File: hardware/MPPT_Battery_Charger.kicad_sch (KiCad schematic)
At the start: 74 parts, among them Q24 SI7414DN-T1-E3, Q25 SI7414DN-T1-E3, Q5 SI2302DDS-T1-GE3, Q5 SI7414DN-T1-E3, Q6 SI7414DN-T1-E3, U22 BQ24650RVAT, U26 LMV321RIYLT, U28 LMV321RIYLT, U4 INA199C1DCKR

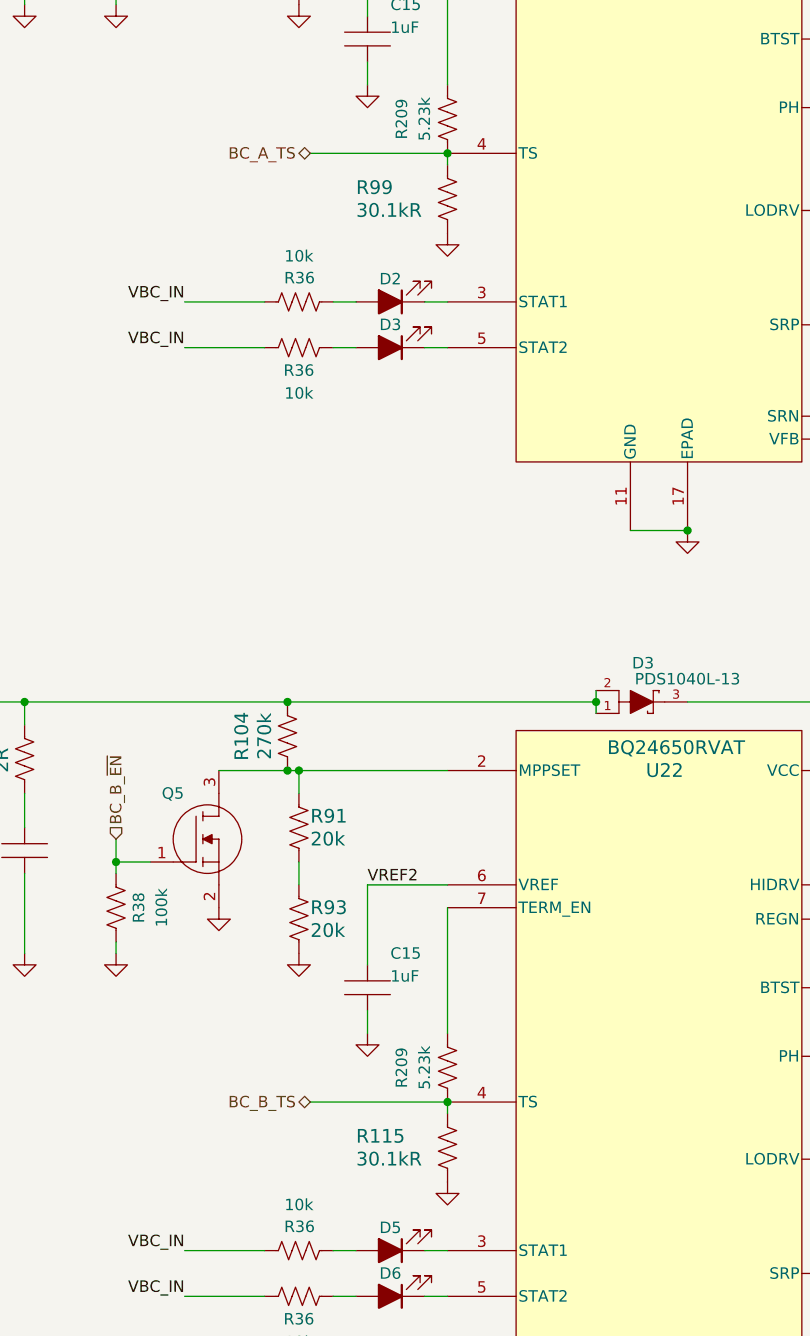
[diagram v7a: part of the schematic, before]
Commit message: hardware: Updating some footprints and 3D models.
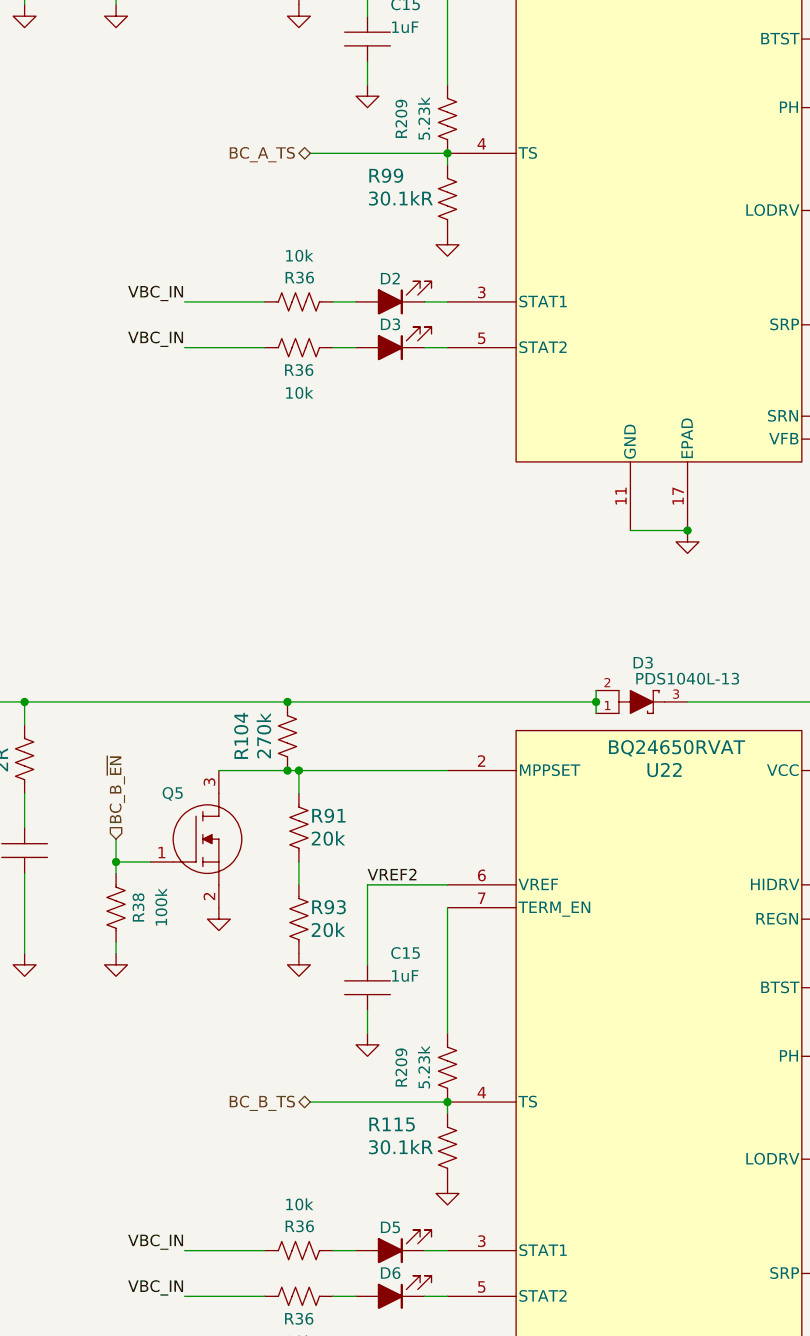
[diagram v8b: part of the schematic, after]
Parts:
- R115, R99: footprint RES_CRCW_0603_VIS -> footprints:CRCW060330K1FKEAHP
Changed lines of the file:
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@@
     )
   )
-  (symbol (lib_name "CRCW060330K1FKEAHP_1") (lib_id "CRCW060330K1FKEAHP:CRCW060330K1FKEAHP") (at 148.59 80.01 90) (unit 1)
+  (symbol (lib_id "CRCW060330K1FKEAHP:CRCW060330K1FKEAHP") (at 149.86 78.74 90) (unit 1)
     (in_bom yes) (on_board yes) (dnp no)
-    (property "Reference" "R99" (at 139.7 72.39 90)
+    (property "Reference" "R99" (at 140.97 71.12 90)
       (effects (font (size 1.524 1.524)) (justify right))
     )
-    (property "Value" "30.1kR" (at 139.7 74.93 90)
+    (property "Value" "30.1kR" (at 140.97 73.66 90)
       (effects (font (size 1.524 1.524)) (justify right))
     )
-    (property "Footprint" "RES_CRCW_0603_VIS" (at 148.59 80.01 0)
+    (property "Footprint" "footprints:CRCW060330K1FKEAHP" (at 149.86 78.74 0)
       (effects (font (size 1.27 1.27) italic) hide)
     )
-    (property "Datasheet" "CRCW060330K1FKEAHP" (at 148.59 80.01 0)
+    (property "Datasheet" "CRCW060330K1FKEAHP" (at 149.86 78.74 0)
       (effects (font (size 1.27 1.27) italic) hide)
     )
@@
     )
   )
-  (symbol (lib_id "CRCW060330K1FKEAHP:CRCW060330K1FKEAHP") (at 148.59 185.42 90) (unit 1)
+  (symbol (lib_id "CRCW060330K1FKEAHP:CRCW060330K1FKEAHP") (at 149.86 184.15 90) (unit 1)
     (in_bom yes) (on_board yes) (dnp no)
-    (property "Reference" "R115" (at 139.7 177.8 90)
+    (property "Reference" "R115" (at 140.97 176.53 90)
       (effects (font (size 1.524 1.524)) (justify right))
     )
-    (property "Value" "30.1kR" (at 139.7 180.34 90)
+    (property "Value" "30.1kR" (at 140.97 179.07 90)
       (effects (font (size 1.524 1.524)) (justify right))
     )
-    (property "Footprint" "RES_CRCW_0603_VIS" (at 148.59 185.42 0)
+    (property "Footprint" "footprints:CRCW060330K1FKEAHP" (at 149.86 184.15 0)
       (effects (font (size 1.27 1.27) italic) hide)
     )
-    (property "Datasheet" "CRCW060330K1FKEAHP" (at 148.59 185.42 0)
+    (property "Datasheet" "CRCW060330K1FKEAHP" (at 149.86 184.15 0)
       (effects (font (size 1.27 1.27) italic) hide)
     )
